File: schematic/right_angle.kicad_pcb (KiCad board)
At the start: 2 copper layers, 82.5 x 20.3 mm, 3 parts, among them J12 Cartridge Port, J13 Cartridge Connector

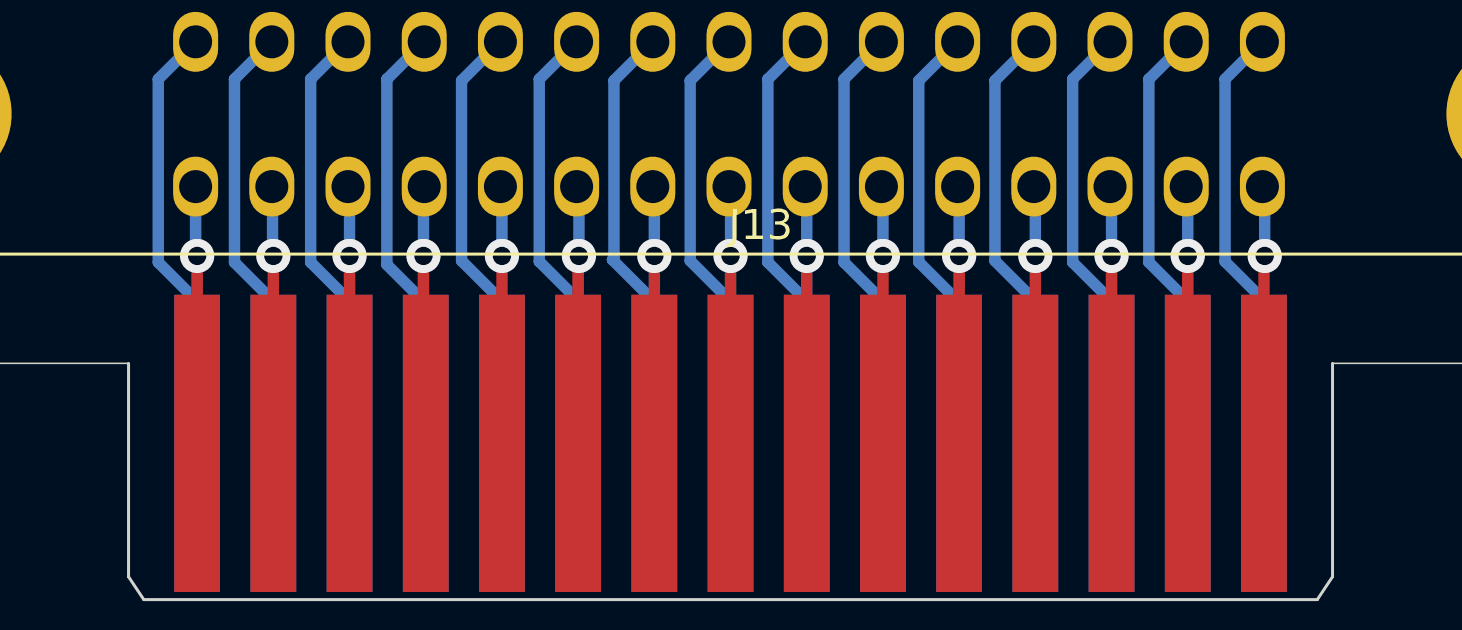
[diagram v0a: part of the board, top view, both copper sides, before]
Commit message: complete ram mirror when banks not enabled.
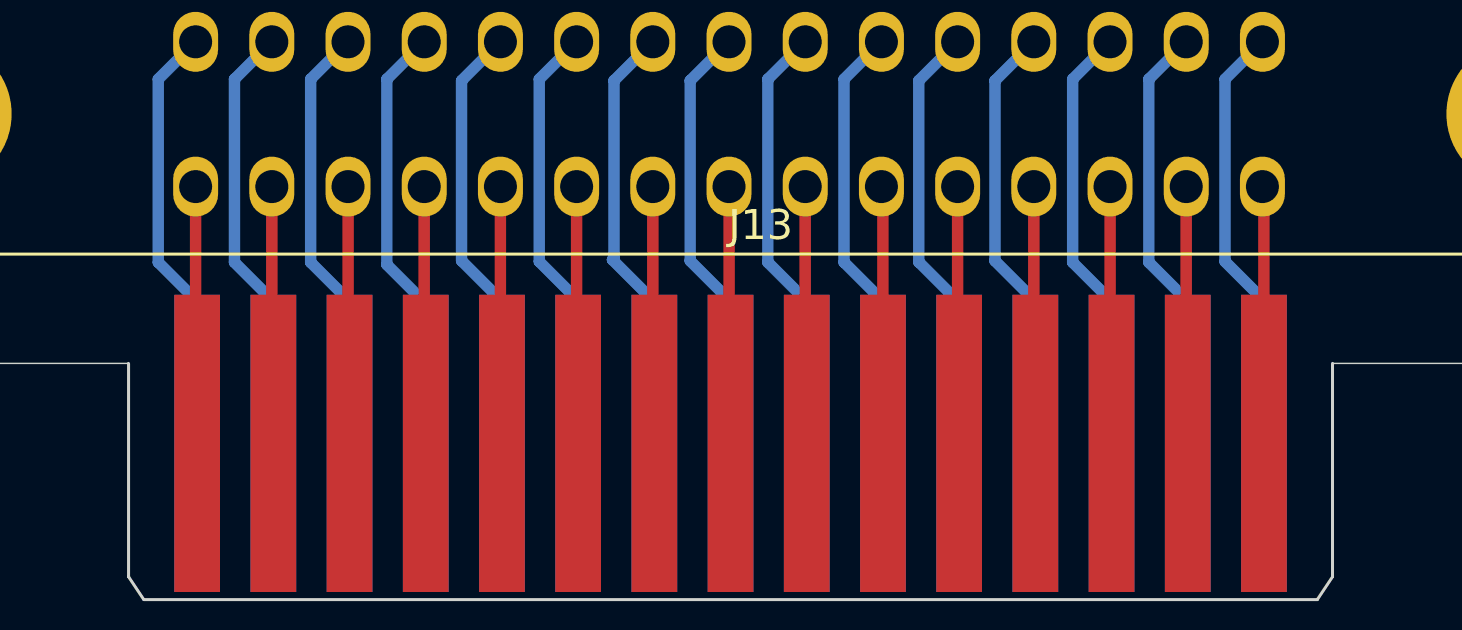
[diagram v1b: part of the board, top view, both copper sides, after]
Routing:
- net Net-(J12-Pin_26): track 8.58 -> 8.65 mm, vias 1 -> 0
- net Net-(J12-Pin_18): track 8.58 -> 8.65 mm, vias 1 -> 0
- net Net-(J12-Pin_8): track 8.60 -> 8.58 mm, vias 1 -> 0
- net Net-(J12-Pin_12): track 8.60 -> 8.58 mm, vias 1 -> 0
- net Net-(J12-Pin_30): track 8.60 -> 8.58 mm, vias 1 -> 0
- net Net-(J12-Pin_6): vias 1 -> 0
- net Net-(J12-Pin_4): vias 1 -> 0
- net Net-(J12-Pin_28): vias 1 -> 0
- net Net-(J12-Pin_24): vias 1 -> 0
- net Net-(J12-Pin_22): vias 1 -> 0
- net Net-(J12-Pin_2): vias 1 -> 0
- net Net-(J12-Pin_16): vias 1 -> 0
- net Net-(J12-Pin_14): vias 1 -> 0
- net Net-(J12-Pin_10): vias 1 -> 0
- net Net-(J12-Pin_20): vias 1 -> 0
